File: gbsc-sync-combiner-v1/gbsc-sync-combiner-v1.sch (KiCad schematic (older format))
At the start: 13 parts, among them J1 DB15_Female_HighDensity_Mount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, J2 JST-XH, J3 JST-XH, U1 74LS86

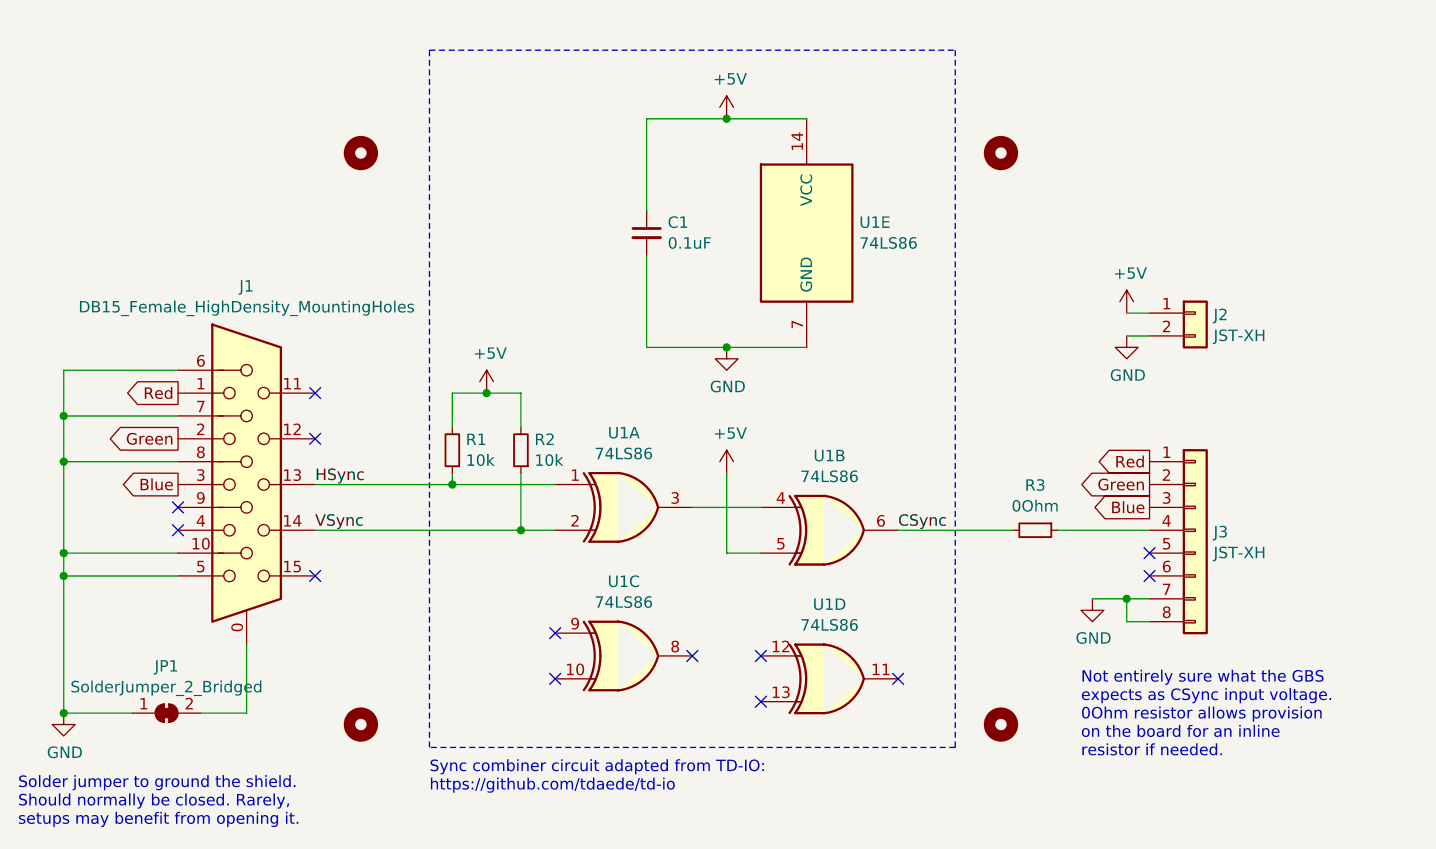
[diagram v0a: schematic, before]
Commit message: Changed existing to -v1 variant, routed board
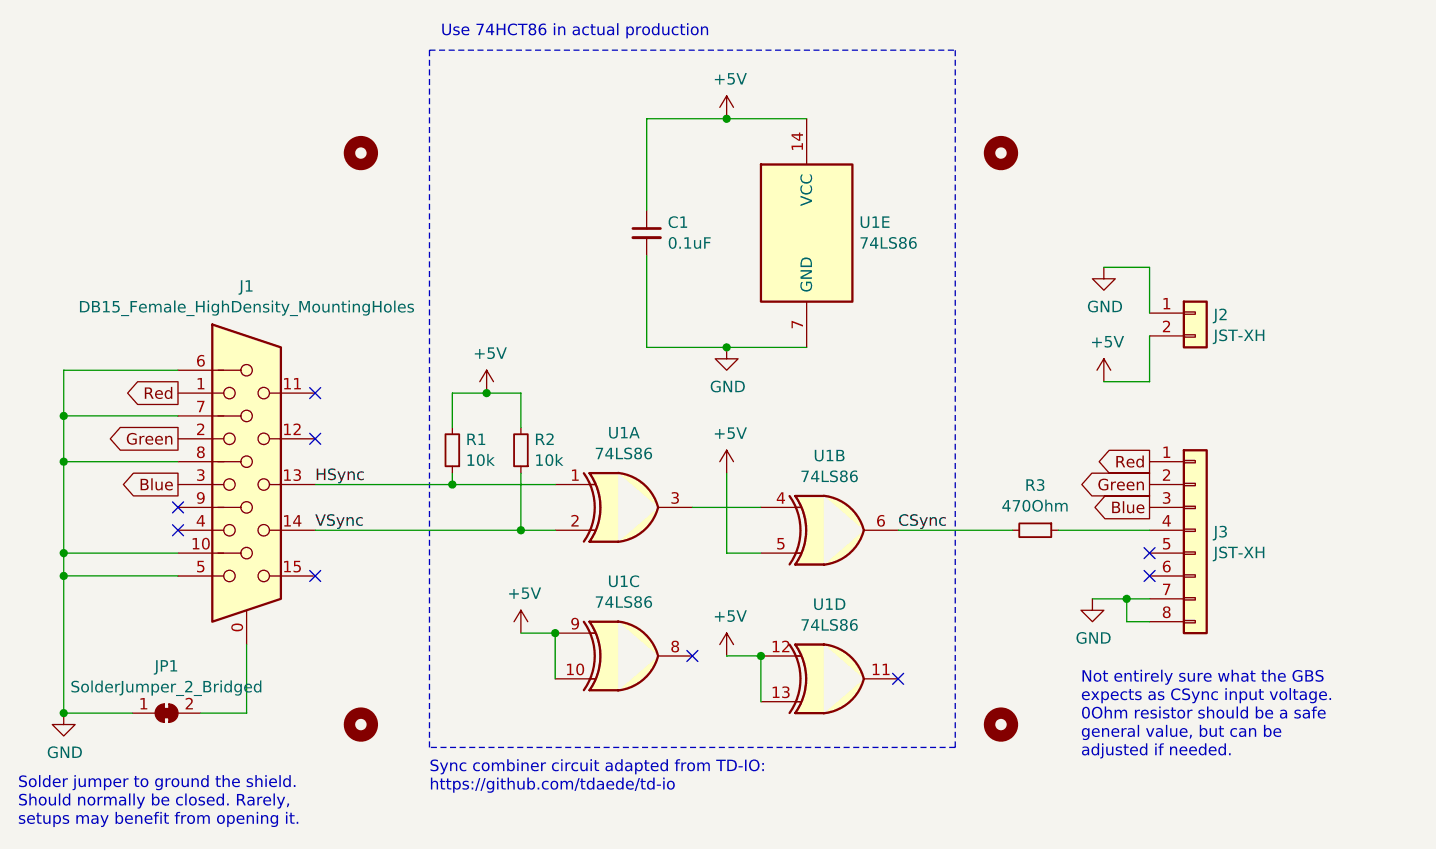
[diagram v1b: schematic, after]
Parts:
- R3: value 0Ohm -> 470Ohm
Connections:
- net +5V: now also J2.2 (Pin_2), U1.10, U1.12, U1.13, U1.9; no longer J2.1 (Pin_1)
- net GND: now also J2.1 (Pin_1); no longer J2.2 (Pin_2)
- no-connect marks 13 -> 9
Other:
- note added: "Not entirely sure what the GBS \nexpects as CSync input voltage.\n0Ohm resistor should be a safe\ngeneral value, but can be \nadjusted if needed."
- note added: "Use 74HCT86 in actual production"
- note removed: "Not entirely sure what the GBS \nexpects as CSync input voltage.\n0Ohm resistor allows provision \non the board for an inline \nresistor if needed."
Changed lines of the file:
@@
 $EndComp
 NoConn ~ 6700 5000
-NoConn ~ 6100 5100
-NoConn ~ 6100 4900
 NoConn ~ 5800 4900
-NoConn ~ 5200 5000
-NoConn ~ 5200 4800
 Wire Wire Line
 	5950 3550 5600 3550
@@
 L power:+5V #PWR0106
 U 1 1 617E835C
-P 7700 3400
-F 0 "#PWR0106" H 7700 3250 50  0001 C CNN
-F 1 "+5V" H 7715 3573 50  0000 C CNN
-F 2 "" H 7700 3400 50  0001 C CNN
-F 3 "" H 7700 3400 50  0001 C CNN
-	1    7700 3400
+P 7600 3700
+F 0 "#PWR0106" H 7600 3550 50  0001 C CNN
+F 1 "+5V" H 7615 3873 50  0000 C CNN
+F 2 "" H 7600 3700 50  0001 C CNN
+F 3 "" H 7600 3700 50  0001 C CNN
+	1    7600 3700
 	1    0    0    -1
 $EndComp
@@
 L power:GND #PWR0107
 U 1 1 617E8C2D
-P 7700 3500
-F 0 "#PWR0107" H 7700 3250 50  0001 C CNN
-F 1 "GND" H 7705 3327 50  0000 C CNN
-F 2 "" H 7700 3500 50  0001 C CNN
-F 3 "" H 7700 3500 50  0001 C CNN
-	1    7700 3500
-	1    0    0    -1
-$EndComp
-Wire Wire Line
-	7800 3400 7700 3400
-Wire Wire Line
-	7800 3500 7700 3500
+P 7600 3200
+F 0 "#PWR0107" H 7600 2950 50  0001 C CNN
+F 1 "GND" H 7605 3027 50  0000 C CNN
+F 2 "" H 7600 3200 50  0001 C CNN
+F 3 "" H 7600 3200 50  0001 C CNN
+	1    7600 3200
+	1    0    0    -1
+$EndComp
 $Comp
 L Connector_Generic:Conn_01x08 J3
@@
 P 7300 4350
 F 0 "R3" V 7104 4350 50  0000 C CNN
-F 1 "0Ohm" V 7195 4350 50  0000 C CNN
+F 1 "470Ohm" V 7195 4350 50  0000 C CNN
 F 2 "Resistor_THT:R_Axial_DIN0207_L6.3mm_D2.5mm_P10.16mm_Horizontal" H 7300 4350 50  0001 C CNN
 F 3 "~" H 7300 4350 50  0001 C CNN
@@
 $EndComp
 Text Notes 7500 5350 0    50   ~ 0
-Not entirely sure what the GBS \nexpects as CSync input voltage.\n0Ohm resistor allows provision \non the board for an inline \nresistor if needed.
+Not entirely sure what the GBS \nexpects as CSync input voltage.\n0Ohm resistor should be a safe\ngeneral value, but can be \nadjusted if needed.
 NoConn ~ 3550 4250
 Wire Wire Line
@@
 	7400 4350 7800 4350
 NoConn ~ 7800 4550
+Wire Wire Line
+	7800 3200 7800 3400
+Wire Wire Line
+	7600 3200 7800 3200
+Wire Wire Line
+	7800 3700 7800 3500
+Wire Wire Line
+	7600 3700 7800 3700
+Text Notes 4700 2200 0    50   ~ 0
+Use 74HCT86 in actual production
+$Comp
+L power:+5V #PWR?
+U 1 1 6184FF3B
+P 5050 4800
+F 0 "#PWR?" H 5050 4650 50  0001 C CNN
+F 1 "+5V" H 5065 4973 50  0000 C CNN
+F 2 "" H 5050 4800 50  0001 C CNN
+F 3 "" H 5050 4800 50  0001 C CNN
+	1    5050 4800
+	1    0    0    -1
+$EndComp
+Wire Wire Line
+	5200 4800 5050 4800
+Wire Wire Line
+	5200 5000 5200 4800
+Connection ~ 5200 4800
+$Comp
+L power:+5V #PWR?
+U 1 1 61854D1C
+P 5950 4900
+F 0 "#PWR?" H 5950 4750 50  0001 C CNN
+F 1 "+5V" H 5965 5073 50  0000 C CNN
+F 2 "" H 5950 4900 50  0001 C CNN
+F 3 "" H 5950 4900 50  0001 C CNN
+	1    5950 4900
+	1    0    0    -1
+$EndComp
+Wire Wire Line
+	6100 4900 5950 4900
+Wire Wire Line
+	6100 5100 6100 4900
+Connection ~ 6100 4900
 $EndSCHEMATC
